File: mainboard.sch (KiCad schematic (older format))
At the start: 67 parts

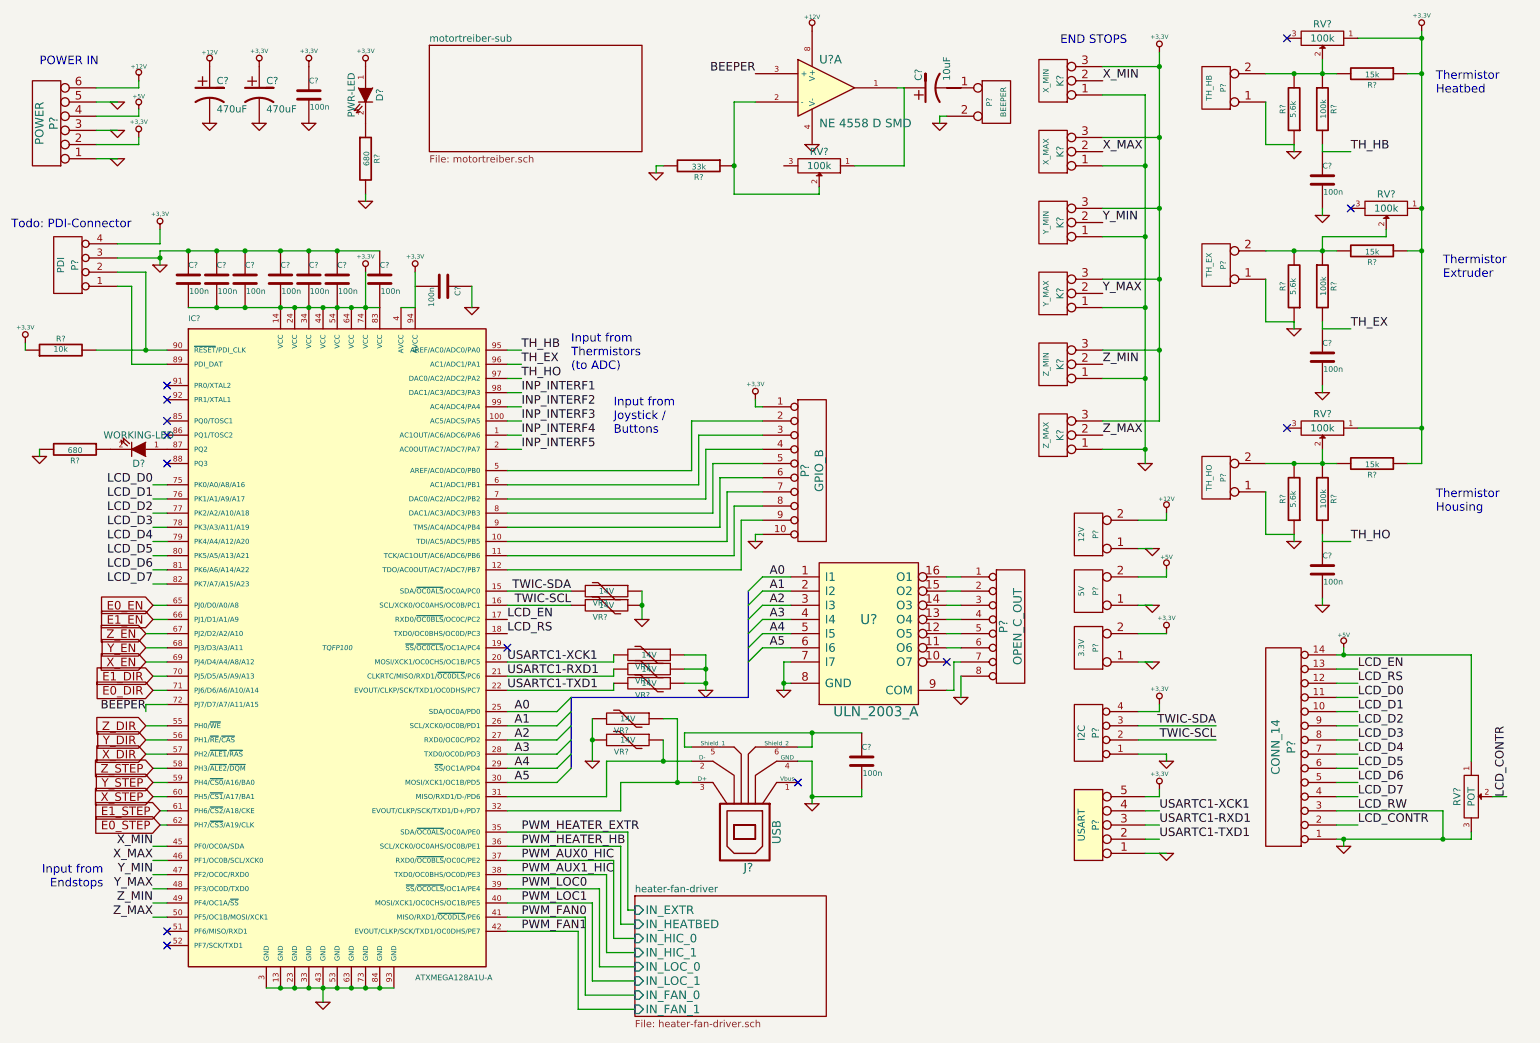
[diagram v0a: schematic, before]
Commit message: Added some LEDs for a better overview what the board is doing when operating; Generated netlist and started to associate footprints
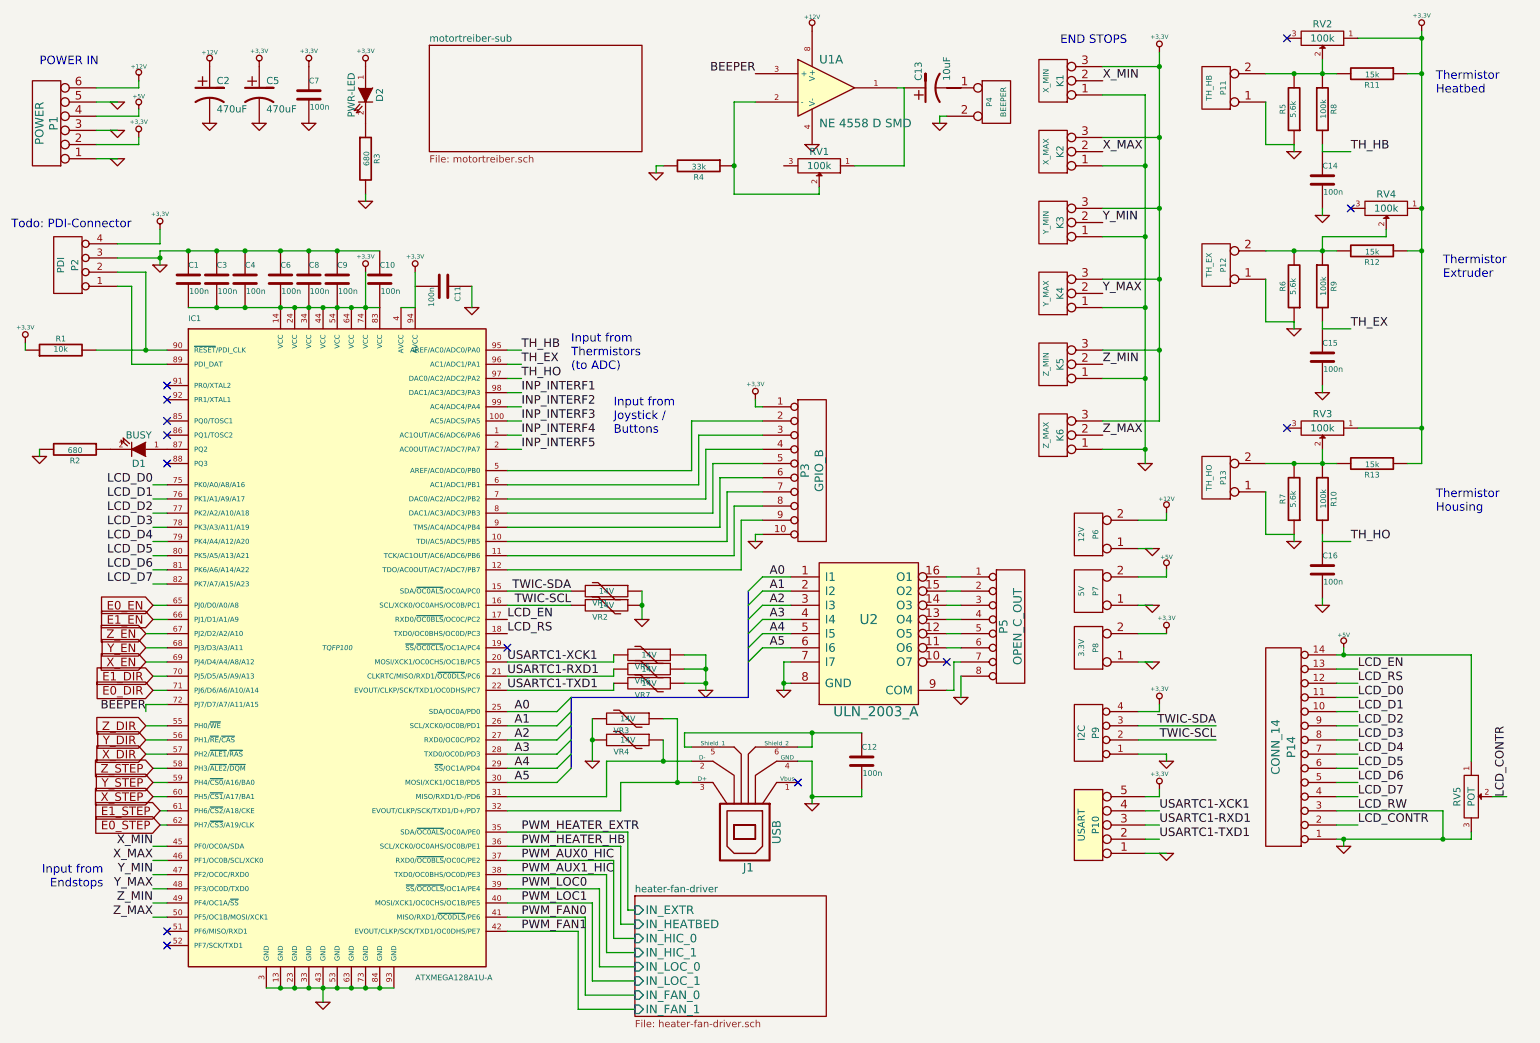
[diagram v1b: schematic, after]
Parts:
- D1: renamed from D?; value WORKING-LED -> BUSY; Color (none) -> Red
- gave numbers to parts that had none: 66

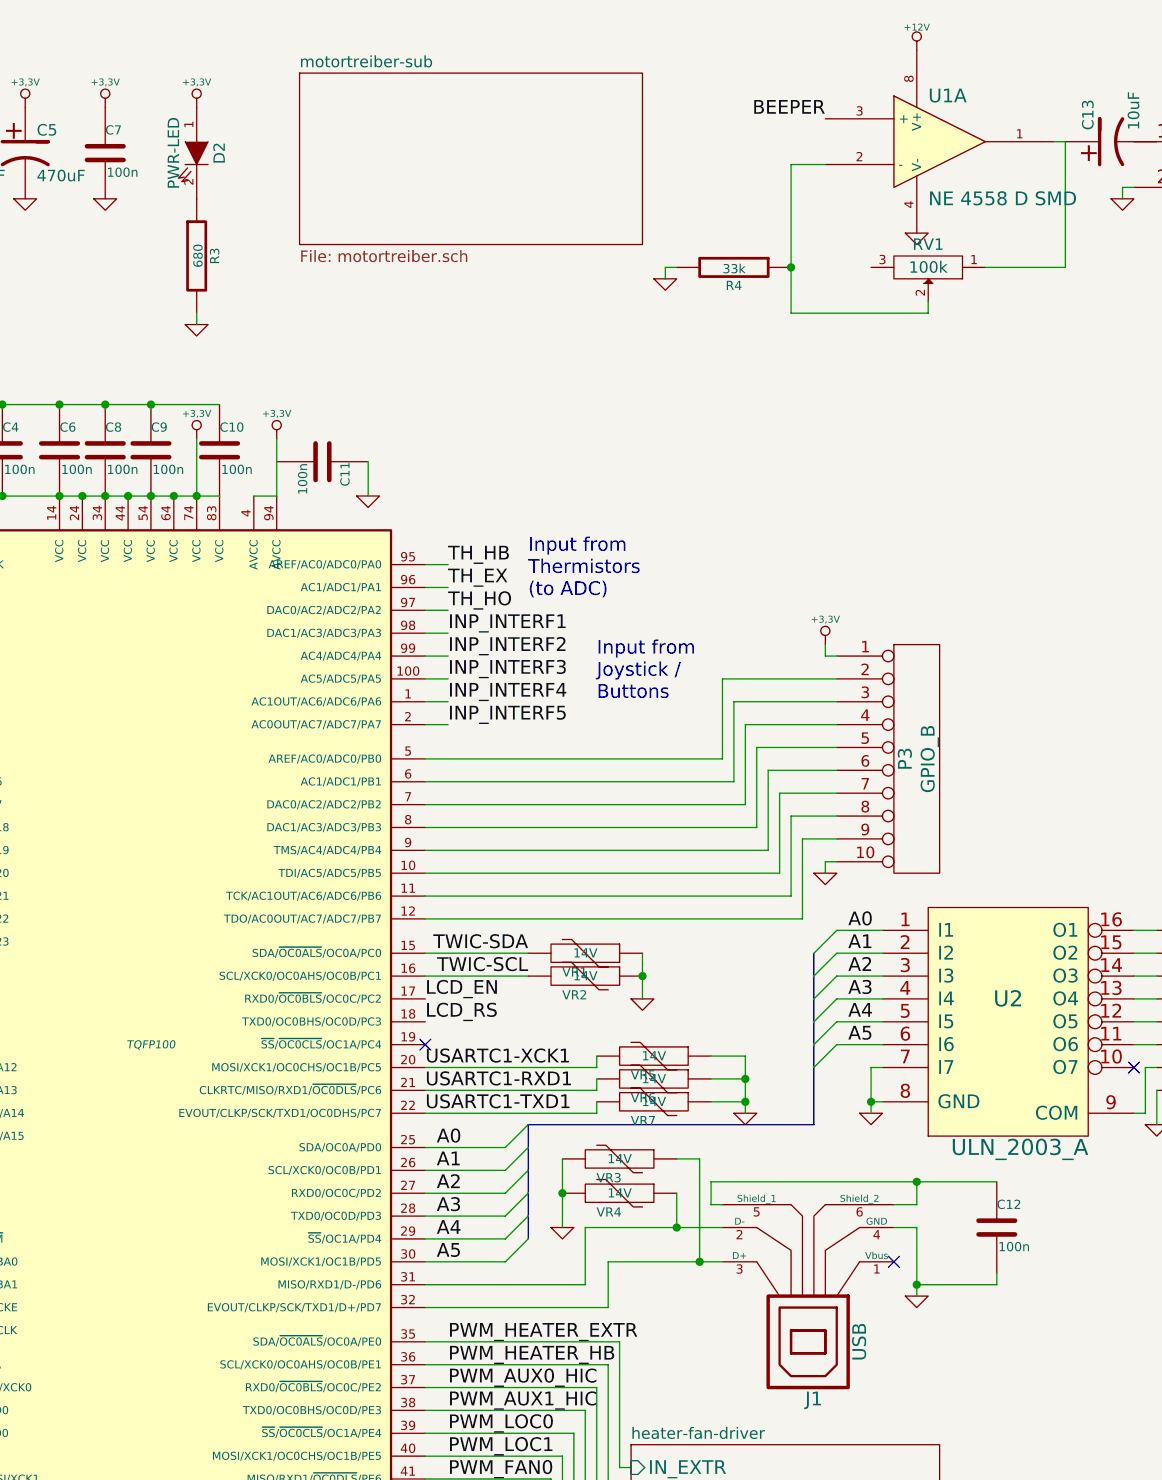
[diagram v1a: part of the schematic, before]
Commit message: Added pullup resistors to I2C interface and protection resistors for USB interface
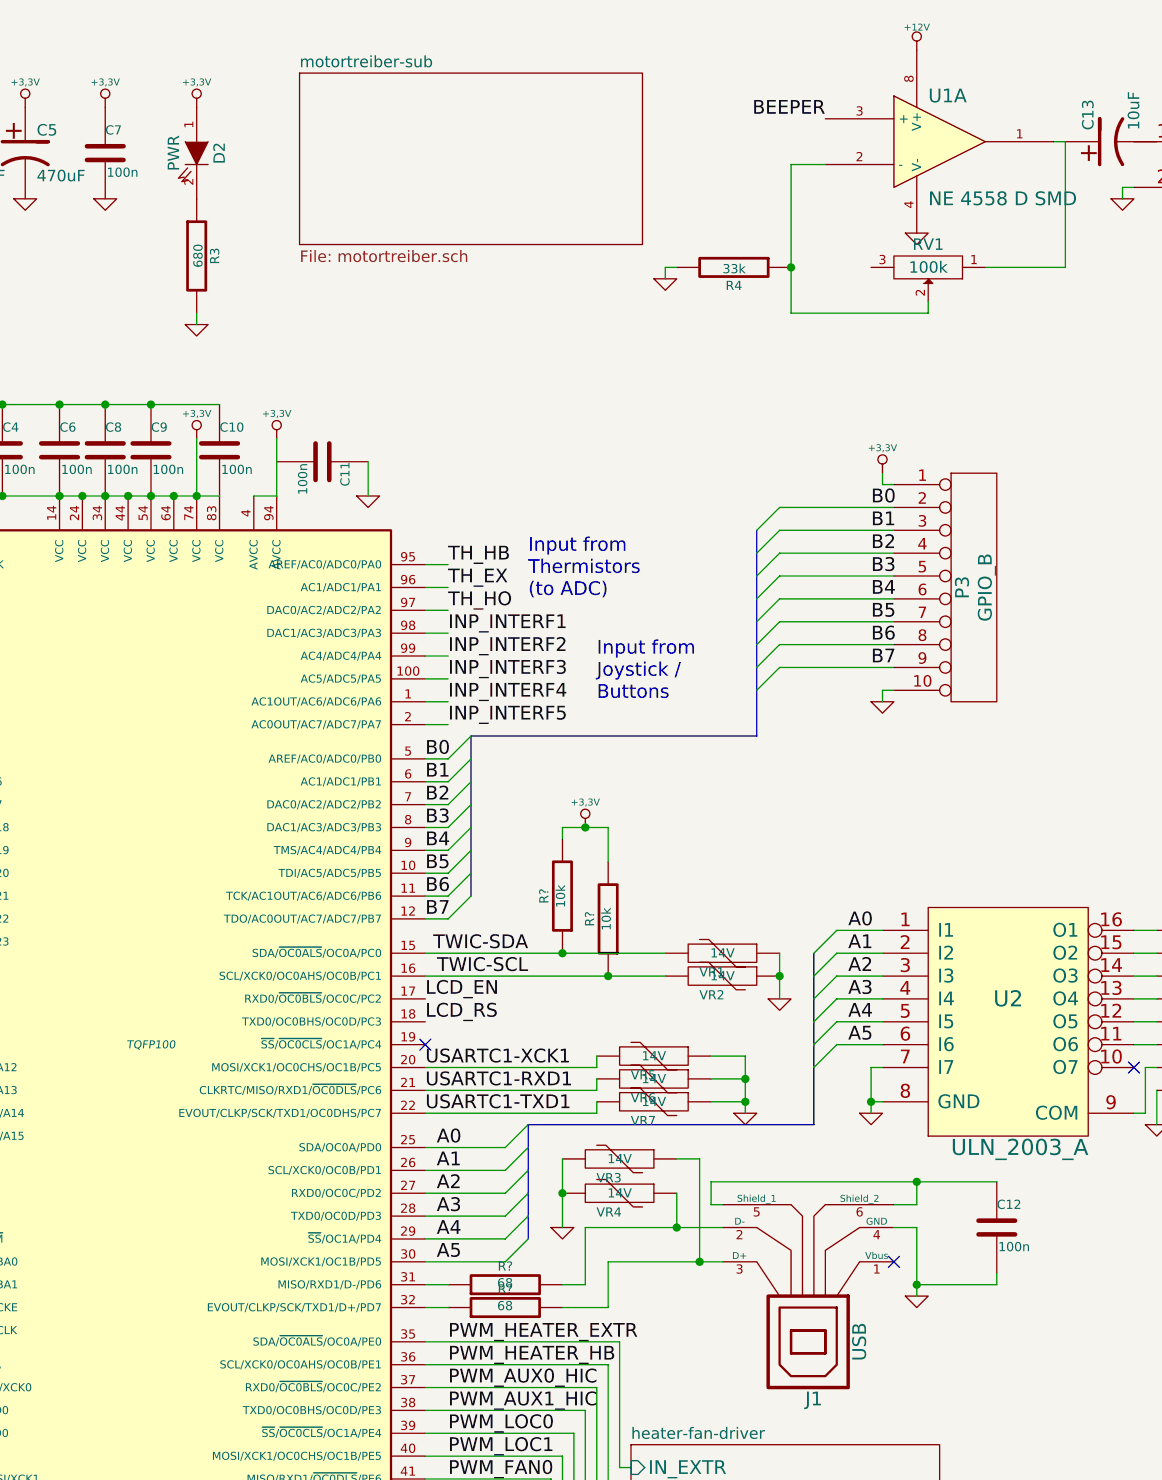
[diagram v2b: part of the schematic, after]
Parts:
- added R? (x2): 10k, symbol R
- added R? (x2): 68, symbol R
- D2: value PWR-LED -> PWR
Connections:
- net +3.3V: now also R?.2, R?.2
- net TWIC-SCL: now also R?.1
- net TWIC-SDA: now also R?.1
- net at J1.2 (D-), VR4.1: now also R?.2; no longer IC1.31 (MISO/RXD1/D-/PD6)
- net at J1.3 (D+), VR3.1: now also R?.2; no longer IC1.32 (EVOUT/CLKP/SCK/TXD1/D+/PD7)
- net B5: now reaches IC1.10 (TDI/AC5/ADC5/PB5), P3.7 (P7)
- net B6: now reaches IC1.11 (TCK/AC1OUT/AC6/ADC6/PB6), P3.8 (P8)
- net B7: now reaches IC1.12 (TDO/AC0OUT/AC7/ADC7/PB7), P3.9 (P9)
- net B0: now reaches IC1.5 (AREF/AC0/ADC0/PB0), P3.2 (P2)
- net B1: now reaches IC1.6 (AC1/ADC1/PB1), P3.3 (P3)
- net B2: now reaches IC1.7 (DAC0/AC2/ADC2/PB2), P3.4 (P4)
- net B3: now reaches IC1.8 (DAC1/AC3/ADC3/PB3), P3.5 (P5)
- net B4: now reaches IC1.9 (TMS/AC4/ADC4/PB4), P3.6 (P6)
- new net: IC1.31 (MISO/RXD1/D-/PD6), R?.1
- new net: IC1.32 (EVOUT/CLKP/SCK/TXD1/D+/PD7), R?.1
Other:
- moved on the sheet: P3, VR1, VR2

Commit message: Added decoupling cap for display supply; Associated most footprints.
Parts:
- added C22: 100n, symbol C
- gave numbers to parts that had none: 4
- renumbered R6 to R10, R7 to R11, R8 to R12, R9 to R13, R10 to R14, R11 to R15, R12 to R16, R13 to R17, R4 to R8, R5 to R9, VR3 to VR1, VR4 to VR2, VR5 to VR3, VR6 to VR4, VR7 to VR5, VR1 to VR6, VR2 to VR7
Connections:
- net +5V: now also C22.1
- net GND: now also C22.2
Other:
- moved on the sheet: D2, R3

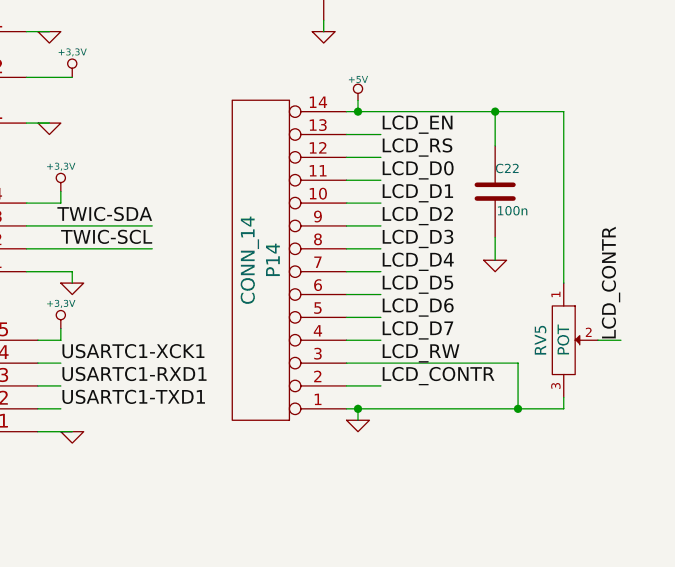
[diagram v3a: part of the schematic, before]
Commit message: Finished footprint association; added footprint for potentiometer
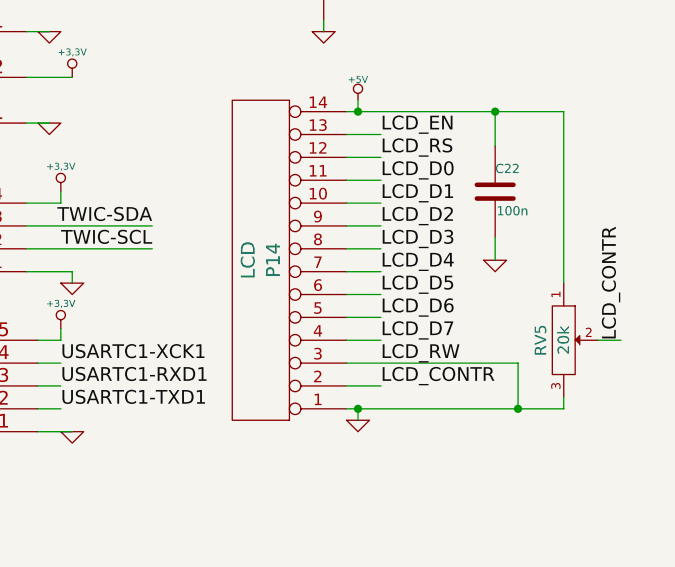
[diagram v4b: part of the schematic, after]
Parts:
- P14: value CONN_14 -> LCD
- RV5: value POT -> 20k
